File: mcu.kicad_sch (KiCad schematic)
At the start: 73 parts, among them J10 Micro_SD_Card, J11 Conn_01x06, J12 Conn_01x02, J14 USB_B, J8 Conn_02x05_Odd_Even, SW1 SW_Push, SW2 SW_Push, U24 REF3033, U25 LPS25HB, U26 STM32F427ZGTx, U27 USBLC6-2SC6, U29 MAX823, Y1 8MHz

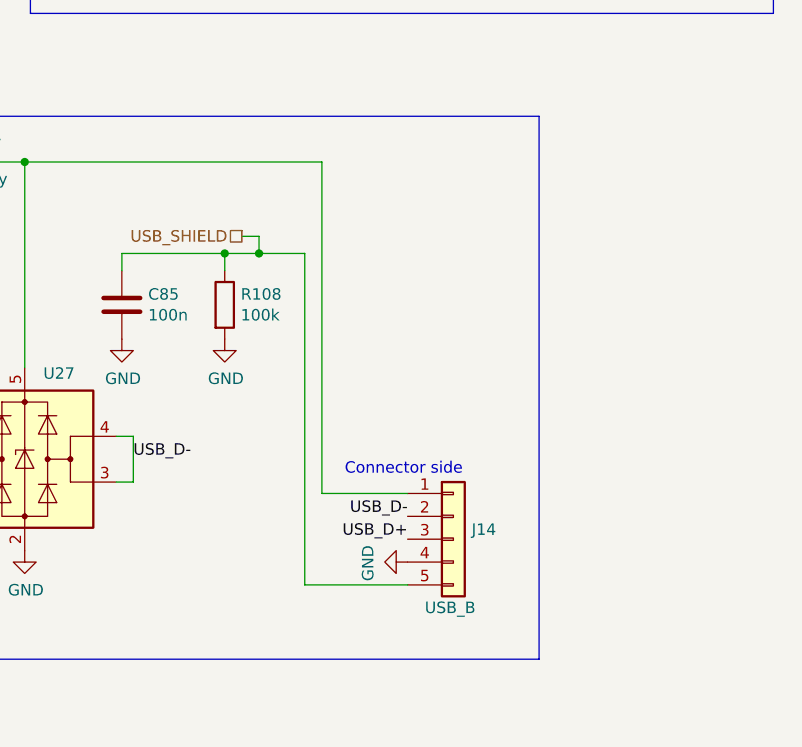
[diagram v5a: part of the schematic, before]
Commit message: Change U9,U10,U14 to SN74LVC2G17DBVR, version as ordered
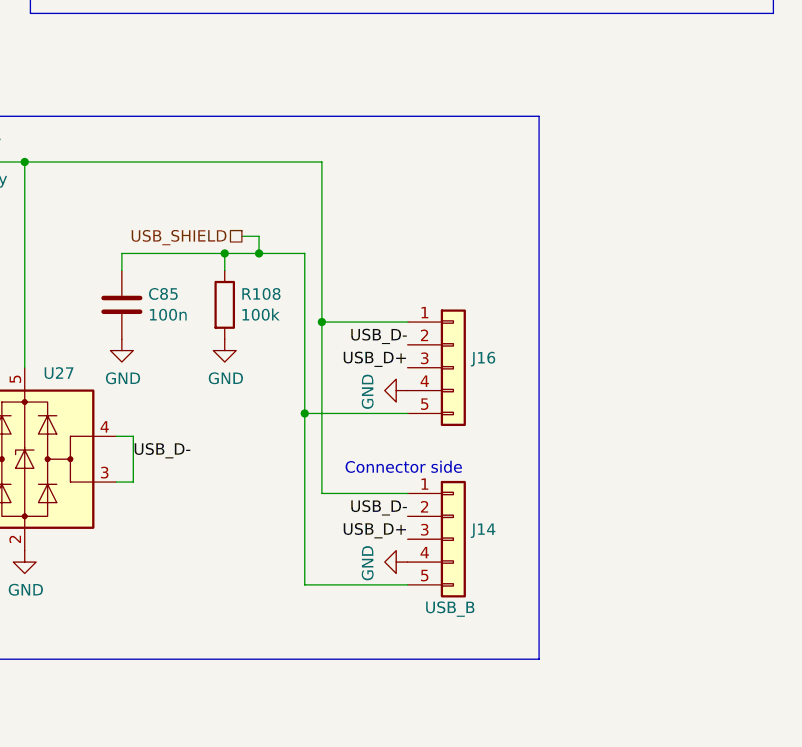
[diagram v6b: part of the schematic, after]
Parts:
- added J16: ~, Connector_PinHeader_2.54mm:PinHeader_1x05_P2.54mm_Vertical, symbol Connector_Generic:Conn_01x05
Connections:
- net GND: now also J16.4 (Pin_4)
- net USB_D+: now also J16.3 (Pin_3)
- net USB_D-: now also J16.2 (Pin_2)
- net USB_SHIELD: now also J16.5 (Pin_5)
- net at D17.2 (A), J14.1 (Pin_1), U27.5 (VBUS): now also J16.1 (Pin_1)
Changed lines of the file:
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@@
   (junction (at 129.54 252.73) (diameter 0) (color 0 0 0 0)
   )
+  (junction (at 314.96 95.885) (diameter 0) (color 0 0 0 0)
+  )
   (junction (at 149.86 64.77) (diameter 0) (color 0 0 0 0)
   )
@@
   (junction (at 206.375 62.865) (diameter 0) (color 0 0 0 0)
   )
+  (junction (at 313.055 106.045) (diameter 0) (color 0 0 0 0)
+  )
   (junction (at 90.805 116.205) (diameter 0) (color 0 0 0 0)
   )
@@
     (stroke (width 0) (type default))
   )
+  (wire (pts (xy 314.96 95.885) (xy 314.96 114.935))
+    (stroke (width 0) (type default))
+  )
   (wire (pts (xy 292.1 108.585) (xy 294.005 108.585))
     (stroke (width 0) (type default))
@@
     (stroke (width 0) (type default))
   )
+  (wire (pts (xy 313.055 106.045) (xy 313.055 125.095))
+    (stroke (width 0) (type default))
+  )
   (polyline (pts (xy 257.81 73.025) (xy 339.09 73.025))
     (stroke (width 0) (type default))
@@
     (stroke (width 0) (type default))
   )
+  (wire (pts (xy 313.055 106.045) (xy 324.485 106.045))
+    (stroke (width 0) (type default))
+  )
   (wire (pts (xy 304.165 90.17) (xy 304.165 88.265))
     (stroke (width 0) (type default))
@@
     (stroke (width 0) (type default))
   )
-  (wire (pts (xy 313.055 88.265) (xy 313.055 125.095))
+  (wire (pts (xy 313.055 88.265) (xy 313.055 106.045))
     (stroke (width 0) (type default))
   )
@@
     (stroke (width 0) (type default))
   )
-  (wire (pts (xy 314.96 78.105) (xy 314.96 114.935))
+  (wire (pts (xy 314.96 78.105) (xy 314.96 95.885))
     (stroke (width 0) (type default))
   )
@@
     (stroke (width 0) (type default))
   )
+  (wire (pts (xy 314.96 95.885) (xy 324.485 95.885))
+    (stroke (width 0) (type default))
+  )
   (wire (pts (xy 336.55 187.325) (xy 335.28 187.325))
     (stroke (width 0) (type default))
@@
     (effects (font (size 1.27 1.27)) (justify right bottom))
   )
+  (label "USB_D+" (at 324.485 100.965 180) (fields_autoplaced)
+    (effects (font (size 1.27 1.27)) (justify right bottom))
+  )
   (label "SD_CS" (at 283.21 167.005 180) (fields_autoplaced)
     (effects (font (size 1.27 1.27)) (justify right bottom))
@@
     (effects (font (size 1.27 1.27)) (justify right bottom))
   )
+  (label "USB_D-" (at 324.485 98.425 180) (fields_autoplaced)
+    (effects (font (size 1.27 1.27)) (justify right bottom))
+  )
   (hierarchical_label "USB_D-" (shape bidirectional) (at 173.99 103.505 0) (fields_autoplaced)
     (effects (font (size 1.27 1.27)) (justify left))
@@
     )
   )
+  (symbol (lib_id "power:GND") (at 324.485 103.505 270) (unit 1)
+    (in_bom yes) (on_board yes) (dnp no)
+    (property "Reference" "#PWR0314" (at 318.135 103.505 0)
+      (effects (font (size 1.27 1.27)) hide)
+    )
+    (property "Value" "GND" (at 320.0908 103.632 0)
+      (effects (font (size 1.27 1.27)))
+    )
+    (property "Footprint" "" (at 324.485 103.505 0)
+      (effects (font (size 1.27 1.27)) hide)
+    )
+    (property "Datasheet" "" (at 324.485 103.505 0)
+      (effects (font (size 1.27 1.27)) hide)
+    )
+    (pin "1")
+    (instances
+      (project "proteus"
+        (path "/d9116601-cae2-4199-827b-70fa136aae51/00000000-0000-0000-0000-00005d99e6ee"
+          (reference "#PWR0314") (unit 1)
+        )
+      )
+    )
+  )
   (symbol (lib_id "Device:R") (at 36.83 67.945 0) (unit 1)
     (in_bom yes) (on_board yes) (dnp no)
@@
         )
       )
+    )
+  )
+  (symbol (lib_id "Connector_Generic:Conn_01x05") (at 329.565 100.965 0) (unit 1)
+    (in_bom no) (on_board yes) (dnp no)
+    (property "Reference" "J16" (at 331.597 99.8982 0)
+      (effects (font (size 1.27 1.27)) (justify left))
+    )
+    (property "Value" "~" (at 326.39 108.585 0)
+      (effects (font (size 1.27 1.27)) (justify left) hide)
+    )
+    (property "Footprint" "Connector_PinHeader_2.54mm:PinHeader_1x05_P2.54mm_Vertical" (at 329.565 100.965 0)
+      (effects (font (size 1.27 1.27)) hide)
+    )
+    (property "Datasheet" "~" (at 329.565 100.965 0)
+      (effects (font (size 1.27 1.27)) hide)
+    )
+    (property "JLCPosOffset" "-1.27,-2.1" (at 329.565 100.965 0)
+      (effects (font (size 1.27 1.27)) hide)
+    )
+    (pin "1")
+    (pin "2")
+    (pin "3")
+    (pin "4")
+    (pin "5")
+    (instances
+      (project "proteus"
+        (path "/d9116601-cae2-4199-827b-70fa136aae51/00000000-0000-0000-0000-00005d99e6ee"
+          (reference "J16") (unit 1)
+        )
+      )
